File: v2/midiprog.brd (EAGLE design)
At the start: 99.1 x 78.7 mm, 54 parts, among them IC1 PIC18F4550_40, IC2 TPIC6B596N, IC4 TPIC6B596N, Q2 2N2222A, Q3 2N2222A, Q4 2N2222A, Q5 8MHz

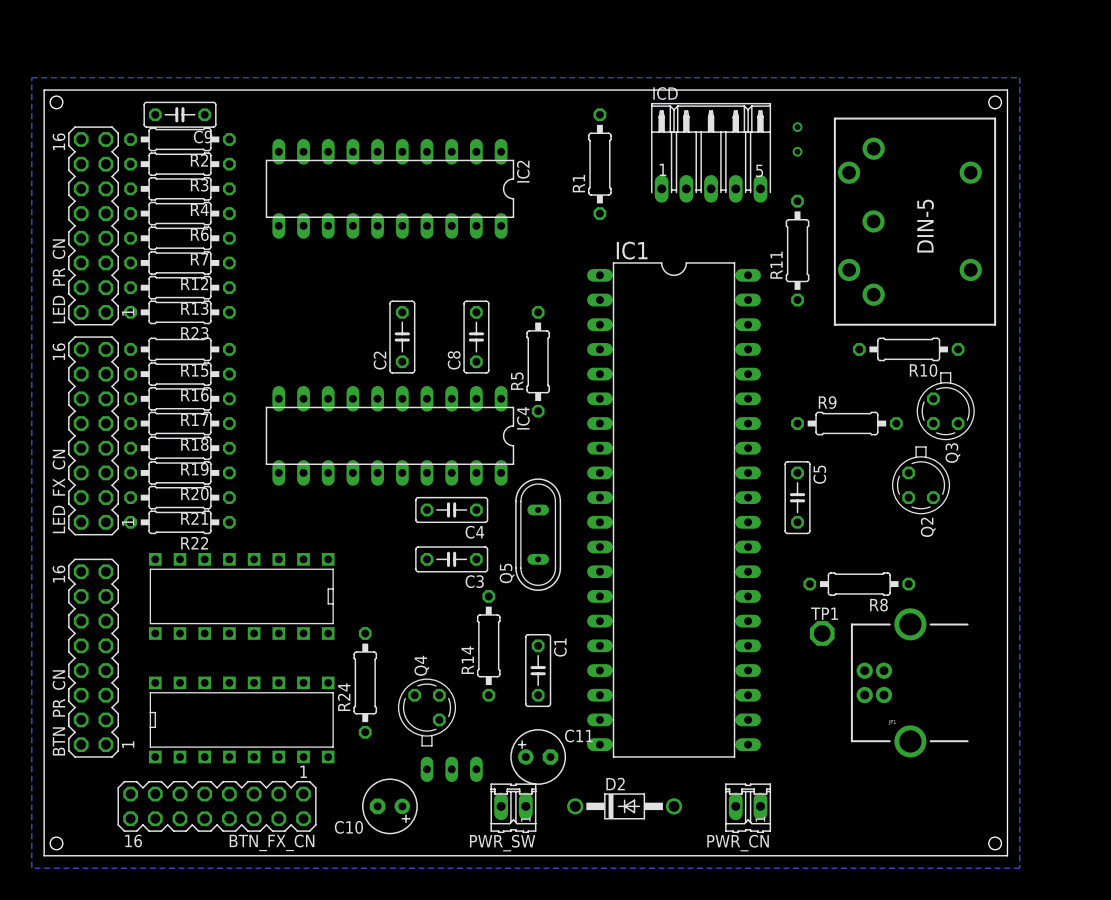
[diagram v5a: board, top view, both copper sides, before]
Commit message: Added C6 and C7 to VDD off muxes.
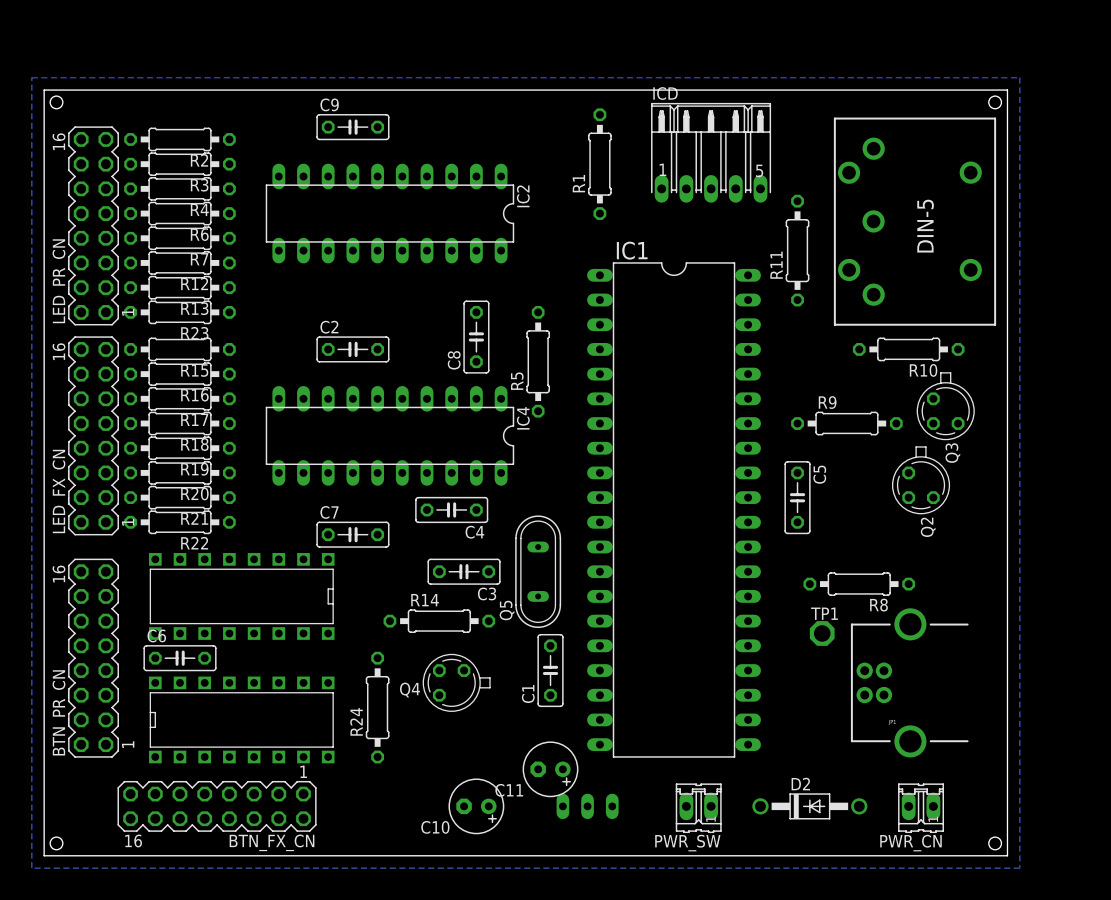
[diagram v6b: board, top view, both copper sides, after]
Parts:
- added C6, C7: .1, rcl:C050-025X075
- moved PWR_SW 19.1 mm to (67.3, 5.08)
- moved D2 19.0 mm to (78.7, 5.08)
- moved C9 17.8 mm to (31.8, 74.9), turned to 0 degrees
- moved PWR_CN 17.8 mm to (90.2, 5.08)
- moved U$3 14.5 mm to (55.9, 5.08)
- moved C10 8.89 mm to (44.5, 5.08)
- moved R14 5.68 mm to (40.6, 24.1), turned to 0 degrees
- moved C2 5.24 mm to (31.8, 52.1), turned to 0 degrees
- moved Q5 3.81 mm to (50.8, 29.2)
- moved Q4 3.59 mm to (41.9, 17.8), turned to 180 degrees
- moved R24 2.84 mm to (34.3, 15.2)
- moved IC2 2.54 mm to (35.6, 66.0)
- moved C11 1.80 mm to (52.1, 8.89), turned to 180 degrees
- moved C3 1.80 mm to (43.2, 29.2)
- moved C1 1.27 mm to (52.1, 19.1), turned to 90 degrees
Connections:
- net GND: now also C6.2, C7.2
- net VDD: now also C6.1, C7.1

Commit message: Cleaning up board.
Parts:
- moved C2 34.5 mm to (59.7, 31.8), turned to 270 degrees
- moved C6 32.6 mm to (44.5, 31.8), turned to 180 degrees
- moved R2 27.4 mm to (40.6, 67.3), turned to 90 degrees
- moved C9 24.4 mm to (35.6, 50.8)
- moved R3 24.4 mm to (38.1, 67.3), turned to 90 degrees
- moved C8 22.9 mm to (36.8, 31.8)
- moved R4 21.6 mm to (35.6, 67.3), turned to 90 degrees
- moved R6 19.1 mm to (33.0, 67.3), turned to 90 degrees
- moved C10 17.8 mm to (62.2, 6.35), turned to 90 degrees
- moved C4 17.6 mm to (50.8, 20.3), turned to 270 degrees
- moved U$2 16.7 mm to (38.1, 15.2), turned to 270 degrees
- moved TP1 15.7 mm to (95.2, 26.7)
- moved C3 15.5 mm to (55.9, 20.3), turned to 270 degrees
- moved BTN_FX_CN 13.7 mm to (25.4, 16.5), turned to 90 degrees
- moved R24 13.5 mm to (43.2, 5.08), turned to 0 degrees
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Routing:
- added copper zone on layer 1, net GND

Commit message: Happy with the LED layouts.
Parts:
- moved LED_PR_CN 44.4 mm to (48.3, 73.7), turned to 0 degrees
- moved LED_FX_CN 33.7 mm to (16.5, 73.7), turned to 0 degrees
- moved IC4 33.4 mm to (14.0, 53.3), turned to 0 degrees
- moved R7 33.1 mm to (47.0, 64.8), turned to 90 degrees
- moved R22 32.4 mm to (7.62, 64.8), turned to 90 degrees
- moved C9 31.4 mm to (5.08, 43.2), turned to 270 degrees
- moved R12 30.9 mm to (44.5, 64.8), turned to 90 degrees
- moved R2 30.2 mm to (52.1, 39.4), turned to 0 degrees
- moved R5 30.1 mm to (27.9, 25.4)
- moved R21 29.5 mm to (10.2, 64.8), turned to 90 degrees
- moved R3 29.0 mm to (52.1, 41.9), turned to 0 degrees
- moved R13 29.0 mm to (41.9, 64.8), turned to 90 degrees
- moved R4 28.2 mm to (52.1, 44.5), turned to 0 degrees
- moved R6 27.9 mm to (52.1, 47.0), turned to 0 degrees
- moved R23 27.4 mm to (39.4, 64.8), turned to 90 degrees
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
